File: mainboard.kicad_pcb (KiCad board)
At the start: 2 copper layers, 150 x 70 mm, 133 parts, among them J1 USB_C_Receptacle_USB2.0_16P, J10 Valve7, J11 AuxPump, J12 MainPump, J13 WaterLevelSensor, J14 OneWireTemp, J15 OneWireTemp, J16 Conn_01x14_MountingPin, J17 FlowSensor, J2 Valve1, J3 Servo, J4 HX711, J5 Valve2, J6 Valve3, J7 Valve4, J8 Valve5, J9 Valve6, Q1 DMN3008SFG, Q10 IRLML2502, Q11 IRLML2502, Q2 DMN3008SFG, Q3 IRLML2502, Q4 IRLML2502, Q5 IRLML2502, Q6 IRLML2502, Q7 IRLML2502, Q8 IRLML2502, Q9 IRLML2502, U1 AP33771, U2 AP62150WU, U3 DRV8870DDAR, U4 AP62150WU, U5 USBLC6-2SC6, U6 ESP32-S3-WROOM-1

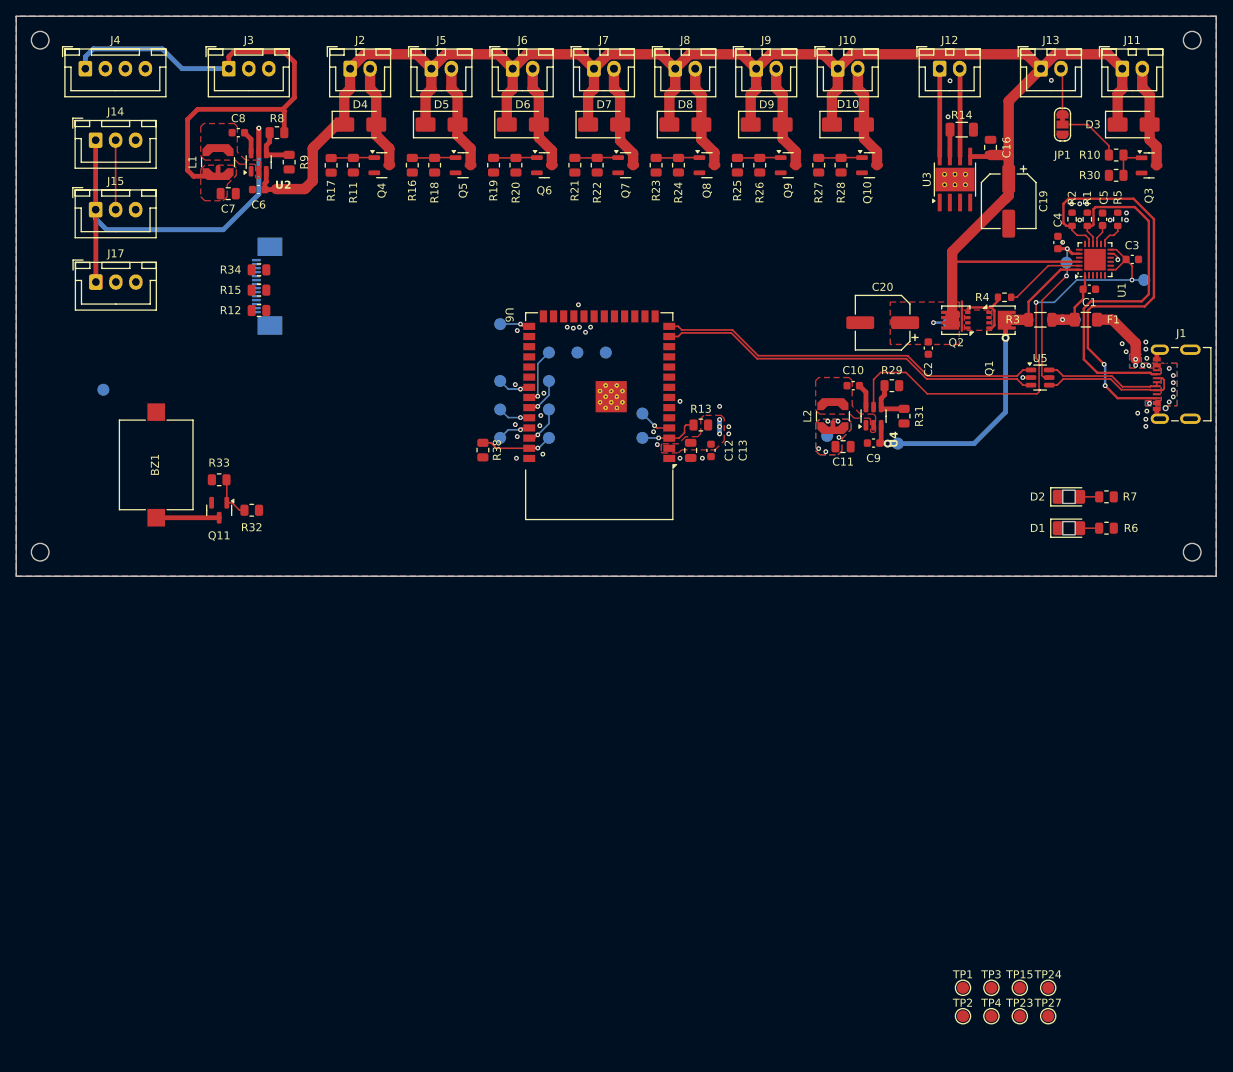
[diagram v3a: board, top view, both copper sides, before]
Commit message: Finalize pin mapping, cleanup and layout
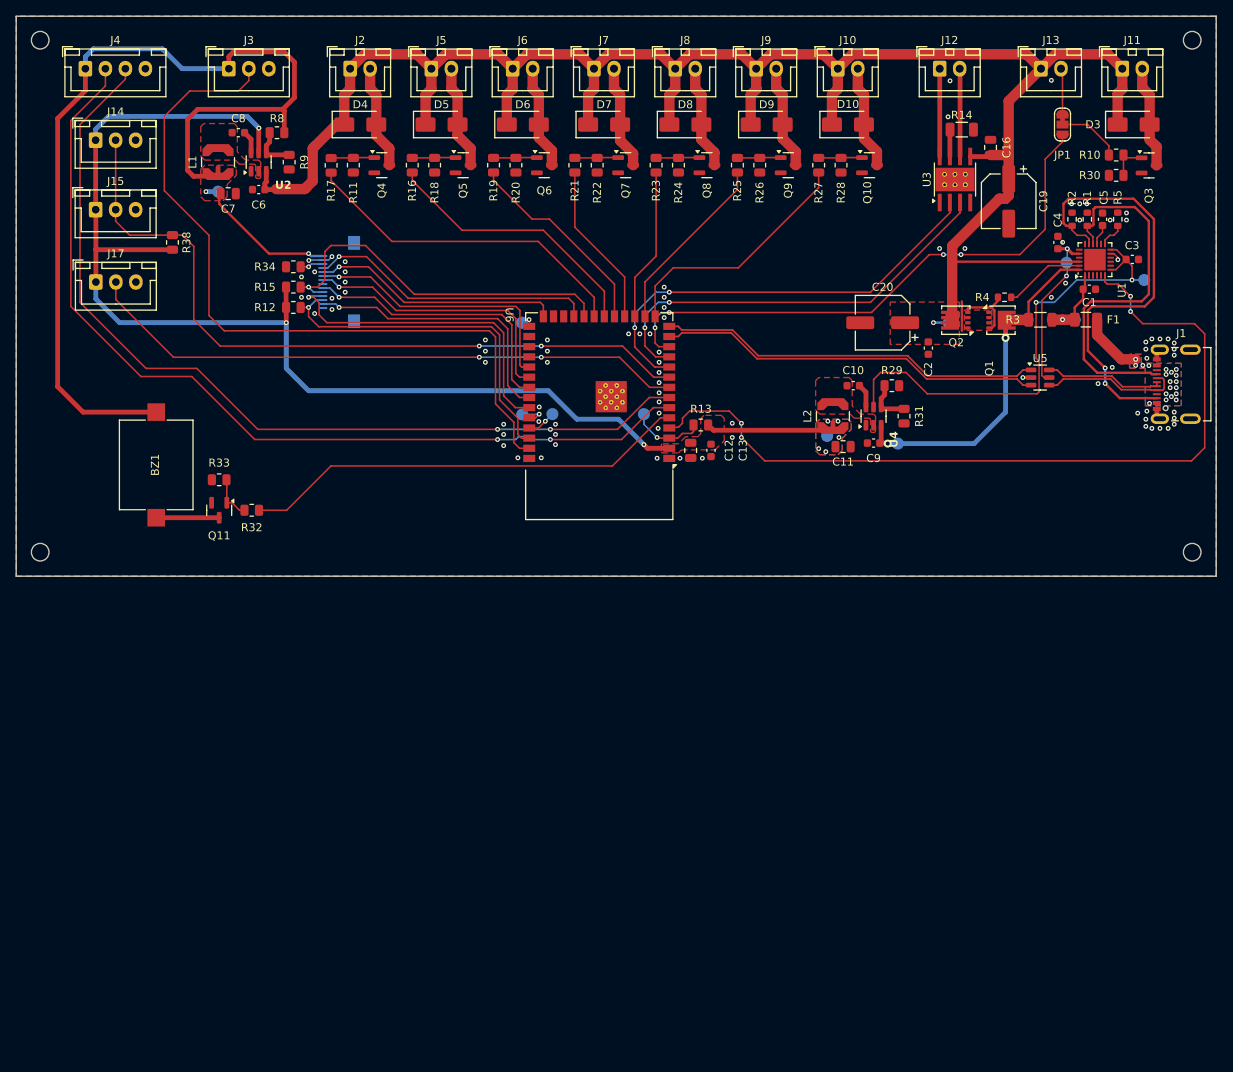
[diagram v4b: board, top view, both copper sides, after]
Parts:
- removed D1: LTST-C230CKT, project:LTST-C230
- removed D2: LTST-C230KGKT, project:LTST-C230
- removed R6: R300, Resistor_SMD:R_0805_2012Metric
- removed R7: R2k7, Resistor_SMD:R_0805_2012Metric
- removed TP1, TP10, TP11, TP12, TP13, TP14, TP15, TP2, TP23, TP24, TP27, TP3, TP4, TP7, TP8, TP9: TestPoint_Small, TestPoint:TestPoint_Pad_D1.5mm
- J16: footprint Connector_FFC-FPC:TE_1-1734839-4_1x14-1MP_P0.5mm_Horizontal -> project:XF2M-1415-1A
- moved R38 46.7 mm to (65.5, 57.3)
- moved TP25 28.6 mm to (71.2, 50.9)
- moved G*** 12.8 mm to (65.0, 80.0)
- moved G*** 12.8 mm to (65.0, 73.0)
- moved TP17 7.18 mm to (113.0, 78.7)
- moved J16 6.99 mm to (84.3, 62.2)
- moved R34 4.31 mm to (80.6, 60.3)
- moved R12 4.31 mm to (80.6, 65.4)
- moved R15 4.31 mm to (80.6, 62.9)
- moved TP5 2.98 mm to (124.5, 78.7)
- moved TP16 2.83 mm to (109.3, 78.8)
- moved TP6 2.73 mm to (109.2, 67.3)
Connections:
- J16 pad 8: /User Interface/LCD_BACKLIGHT -> unconnected-(J16-Pin_8-Pad8)
- J16 pad MP: unconnected-(J16-MountPin-PadMP) -> GND
- U6 pad 10: /MCU/LCD_MOSI -> /MCU/MAIN_PUMP_CTRL2
- U6 pad 11: /MCU/LCD_MISO -> /MCU/MAIN_PUMP_CTRL1
- U6 pad 12: /MCU/LCD_RS -> /MCU/AUX_PUMP_CTRL
- U6 pad 22: /MCU/LCD_SCK -> /MCU/LCD_TOUCH_SCL
- U6 pad 23: /MCU/LCD_TOUCH_RESET -> /MCU/LCD_RESET
- U6 pad 26: /MCU/LCD_TOUCH_INT -> /MCU/LCD_RS
- U6 pad 31: /MCU/LCD_TOUCH_SDA -> /MCU/LCD_MOSI
- U6 pad 32: /MCU/LCD_TOUCH_SCL -> /MCU/LCD_SCK
- U6 pad 33: /MCU/SERVO_CTRL -> /MCU/LCD_MISO
- U6 pad 34: /MCU/HX711_DAT -> /MCU/LCD_TOUCH_INT
- U6 pad 35: /MCU/HX711_CLK -> /MCU/LCD_TOUCH_RESET
- U6 pad 38: /MCU/BUZZER -> /MCU/LCD_TOUCH_SDA
- U6 pad 39: /MCU/1WIRE_TEMP -> /MCU/SERVO_CTRL
- U6 pad 5: /MCU/AUX_PUMP_CTRL -> /MCU/BUZZER
- U6 pad 6: /MCU/FLOW_SENSOR -> /MCU/HX711_CLK
- U6 pad 7: /MCU/MAIN_PUMP_CTRL1 -> /MCU/HX711_DAT
- U6 pad 8: /MCU/MAIN_PUMP_CTRL2 -> /MCU/FLOW_SENSOR
- U6 pad 9: /MCU/LCD_RESET -> /MCU/1WIRE_TEMP
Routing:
- net /MCU/HX711_CLK: track 4.88 -> 115.1 mm, vias 1 -> 2
- net /MCU/HX711_DAT: track 7.17 -> 113.4 mm, vias 1 -> 2
- net +3.3V: track 55.9 -> 159.6 mm, vias 9 -> 8
- net /Power/FAULT: track 4.10 -> 103.7 mm, vias 1 -> 4
- net /MCU/SERVO_CTRL: track 4.15 -> 94.4 mm, vias 1 -> 0
- net /MCU/FLOW_SENSOR: track 0.00 -> 75.9 mm, vias 0 -> 2
- net /MCU/1WIRE_TEMP: track 17.8 -> 92.8 mm, vias 1 -> 2
- net +5V: track 64.9 -> 138.0 mm, vias 0 -> 2
- net /MCU/AUX_PUMP_CTRL: track 0.00 -> 71.1 mm, vias 0 -> 4
- net /MCU/MAIN_PUMP_CTRL2: track 0.00 -> 55.4 mm, vias 0 -> 2
- net /MCU/MAIN_PUMP_CTRL1: track 0.00 -> 53.4 mm, vias 0 -> 2
- net /MCU/BUZZER: track 4.99 -> 56.1 mm, vias 1 -> 0
- net /MCU/LCD_TOUCH_SCL: track 0.00 -> 46.3 mm, vias 0 -> 1
- net /MCU/LCD_TOUCH_SDA: track 0.00 -> 44.1 mm, vias 0 -> 1
- net /MCU/VALVE1_CTRL: track 0.00 -> 42.3 mm
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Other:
- board text removed: "Fault"

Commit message: Re-annotate parts by board
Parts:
- renumbered C8 to C1, C20 to C10, C2 to C11, C10 to C12, C11 to C13, C9 to C14, C12 to C15, C13 to C16, C16 to C2, C7 to C3, C6 to C4, C19 to C5, C5 to C6, C4 to C7, C3 to C8, C1 to C9, D4 to D1, D5 to D2, D6 to D3, D7 to D4, D8 to D5, D9 to D6, D10 to D7, D3 to D8, H4 to H3, H3 to H4, J4 to J1, J12 to J10, J13 to J11, J11 to J12, J14 to J13, J15 to J14, J17 to J15, J1 to J16, J16 to J17, J3 to J2, J2 to J3, J5 to J4, J6 to J5, J7 to J6, J8 to J7, J9 to J8, J10 to J9, Q4 to Q1, Q1 to Q10, Q5 to Q2, Q6 to Q3, Q7 to Q4, Q8 to Q5, Q9 to Q6, Q10 to Q7, Q3 to Q8, Q2 to Q9, R8 to R1, R21 to R10, R22 to R11, R23 to R12, R24 to R13, R25 to R14, R26 to R15, R27 to R16, R28 to R17, R17 to R18, R30 to R19, R14 to R2, R2 to R20, R1 to R21, R5 to R22, R38 to R23, R34 to R24, R15 to R25, R4 to R26, R12 to R27, R3 to R28, R10 to R3, R31 to R30, R13 to R31, R33 to R32, R32 to R33, R9 to R4, R11 to R5, R16 to R6, R18 to R7, R19 to R8, R20 to R9, TP25 to TP1, TP26 to TP10, TP19 to TP11, TP22 to TP2, TP21 to TP3, TP18 to TP4, TP20 to TP5, TP5 to TP7, TP17 to TP8, TP16 to TP9, U2 to U1, U3 to U2, U1 to U3, U5 to U4, U6 to U5, U4 to U6

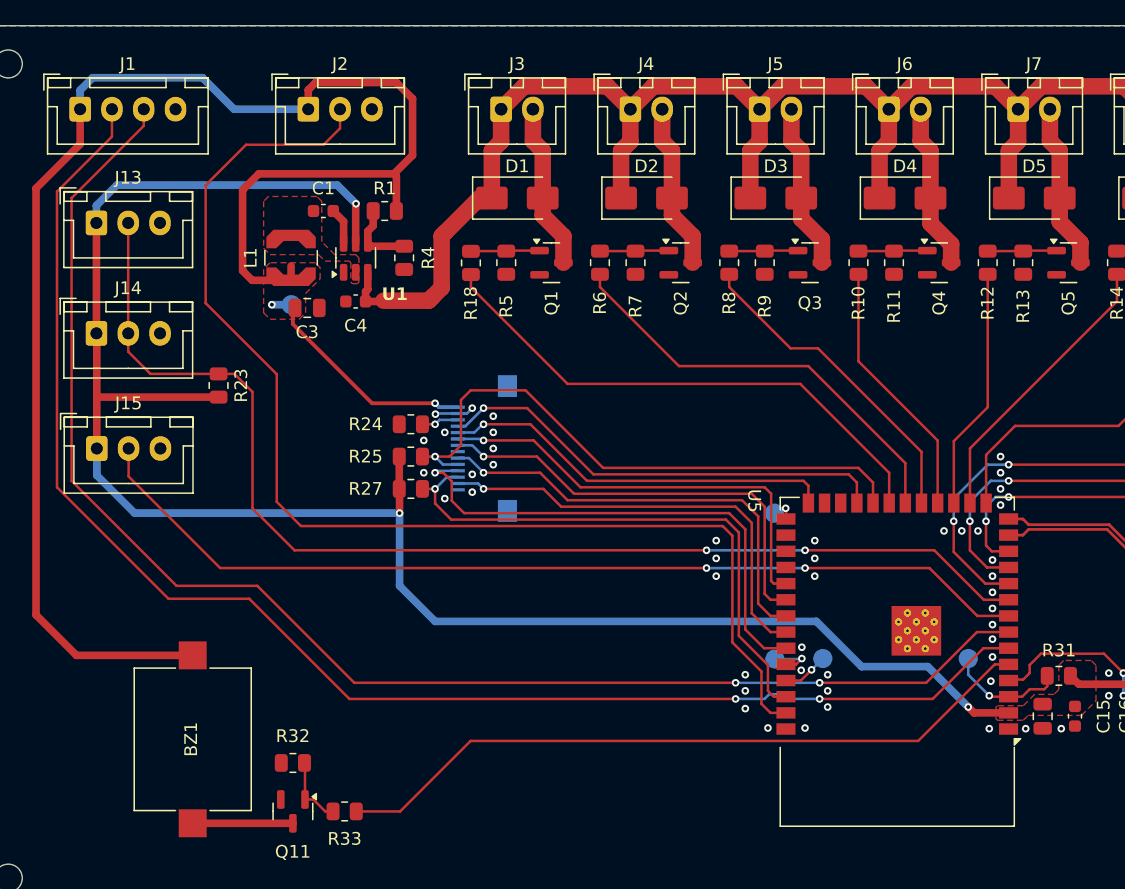
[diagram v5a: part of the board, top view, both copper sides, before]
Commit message: Finish integration of TFT interface
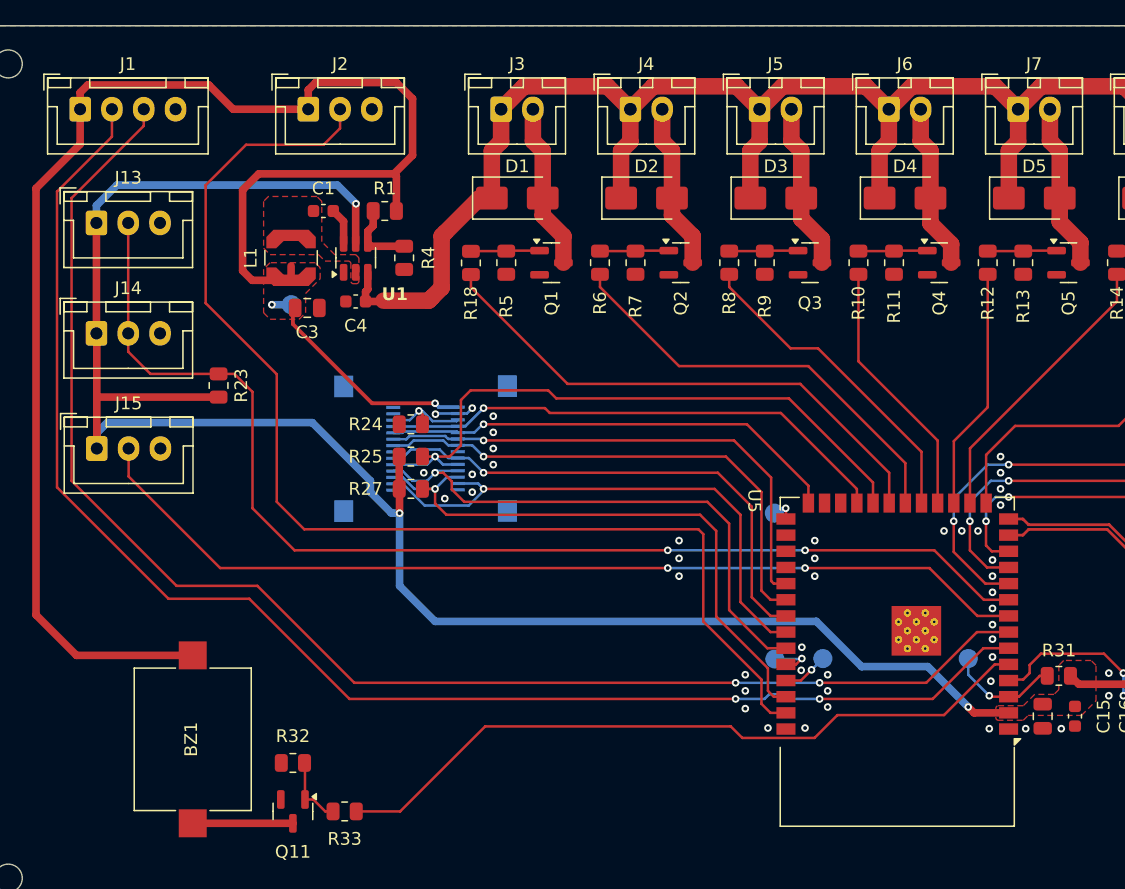
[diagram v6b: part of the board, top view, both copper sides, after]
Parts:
- added J18: Conn_01x14_MountingPin, project:XF2M-1415-1A, B.Cu at (79.3, 62.3)
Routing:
- net /MCU/LCD_TOUCH_INT: track 34.8 -> 43.1 mm
- net /MCU/LCD_MOSI: track 34.5 -> 40.5 mm
- net /MCU/LCD_SCK: track 34.8 -> 40.8 mm
- net /MCU/LCD_MISO: track 35.0 -> 40.7 mm
- net /MCU/LCD_RS: track 31.2 -> 36.3 mm
- net /MCU/LCD_RESET: track 36.0 -> 40.8 mm
- net /User Interface/LCD_CS: track 2.92 -> 6.91 mm
- net /MCU/LCD_TOUCH_SCL: track 46.3 -> 49.9 mm
- net /MCU/LCD_TOUCH_RESET: track 40.6 -> 43.4 mm
- net /MCU/LCD_TOUCH_SDA: track 44.1 -> 46.8 mm
- net +3.3V: track 159.6 -> 161.3 mm
- net /MCU/SERVO_CTRL: track 94.4 -> 93.2 mm
- net /MCU/BUZZER: track 56.1 -> 56.8 mm
- net +5V: track 138.0 -> 137.4 mm
- net GND: vias 86 -> 84
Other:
- board text added: "openautolab mainboard rev.2"
